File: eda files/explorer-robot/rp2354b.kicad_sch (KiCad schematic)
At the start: 34 parts, among them J1 Conn_01x03, SW1 SW_Push, U1 RP2354B, U2 AMS1117-3.3, Y1 ABM8-272-T3

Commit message: Add LiDAR power and UART interface
Add a new lidar schematic sheet with a 4-pin connector, an
AO3400A low-side MOSFET for power switching, and gate pull
resistors. Wire LIDAR_PWR, LIDAR_TX, and LIDAR_RX hierarchical
labels into the MCU sheet and update designators.

Also shorten connector value labels to BAT, LED, and MBR.
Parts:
- J1: value Conn_01x03 -> DBG
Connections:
- net LIDAR_RX: now reaches U1.11 (GPIO12)
- net LIDAR_PWR: now reaches U1.27 (GPIO26)
- net LIDAR_TX: now reaches U1.78 (GPIO1)
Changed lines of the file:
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@@
 	(wire
 		(pts
+			(xy 148.59 102.87) (xy 148.59 105.41)
+		)
+		(stroke
+			(width 0)
+			(type default)
+		)
+	)
+	(wire
+		(pts
 			(xy 264.16 33.02) (xy 264.16 34.29)
 		)
@@
 	(wire
 		(pts
+			(xy 184.15 102.87) (xy 184.15 105.41)
+		)
+		(stroke
+			(width 0)
+			(type default)
+		)
+	)
+	(wire
+		(pts
 			(xy 55.88 24.13) (xy 59.69 24.13)
 		)
@@
 	(wire
 		(pts
+			(xy 120.65 102.87) (xy 120.65 105.41)
+		)
+		(stroke
+			(width 0)
+			(type default)
+		)
+	)
+	(wire
+		(pts
 			(xy 123.19 31.75) (xy 130.81 31.75)
 		)
@@
 		)
 	)
+	(hierarchical_label "LIDAR_PWR"
+		(shape output)
+		(at 184.15 102.87 90)
+		(effects
+			(font
+				(size 1.27 1.27)
+			)
+			(justify left)
+		)
+	)
 	(hierarchical_label "ICM-20948_CS"
 		(shape output)
@@
 		)
 	)
+	(hierarchical_label "LIDAR_RX"
+		(shape output)
+		(at 148.59 102.87 90)
+		(effects
+			(font
+				(size 1.27 1.27)
+			)
+			(justify left)
+		)
+	)
 	(hierarchical_label "MOT.B.IN.2"
 		(shape output)
@@
 		)
 	)
+	(hierarchical_label "LIDAR_TX"
+		(shape input)
+		(at 120.65 102.87 90)
+		(effects
+			(font
+				(size 1.27 1.27)
+			)
+			(justify left)
+		)
+	)
 	(hierarchical_label "LED_R"
 		(shape output)
@@
 			)
 		)
-		(property "Value" "Conn_01x03"
+		(property "Value" "DBG"
 			(at 26.416 175.26 90)
 			(show_name no)

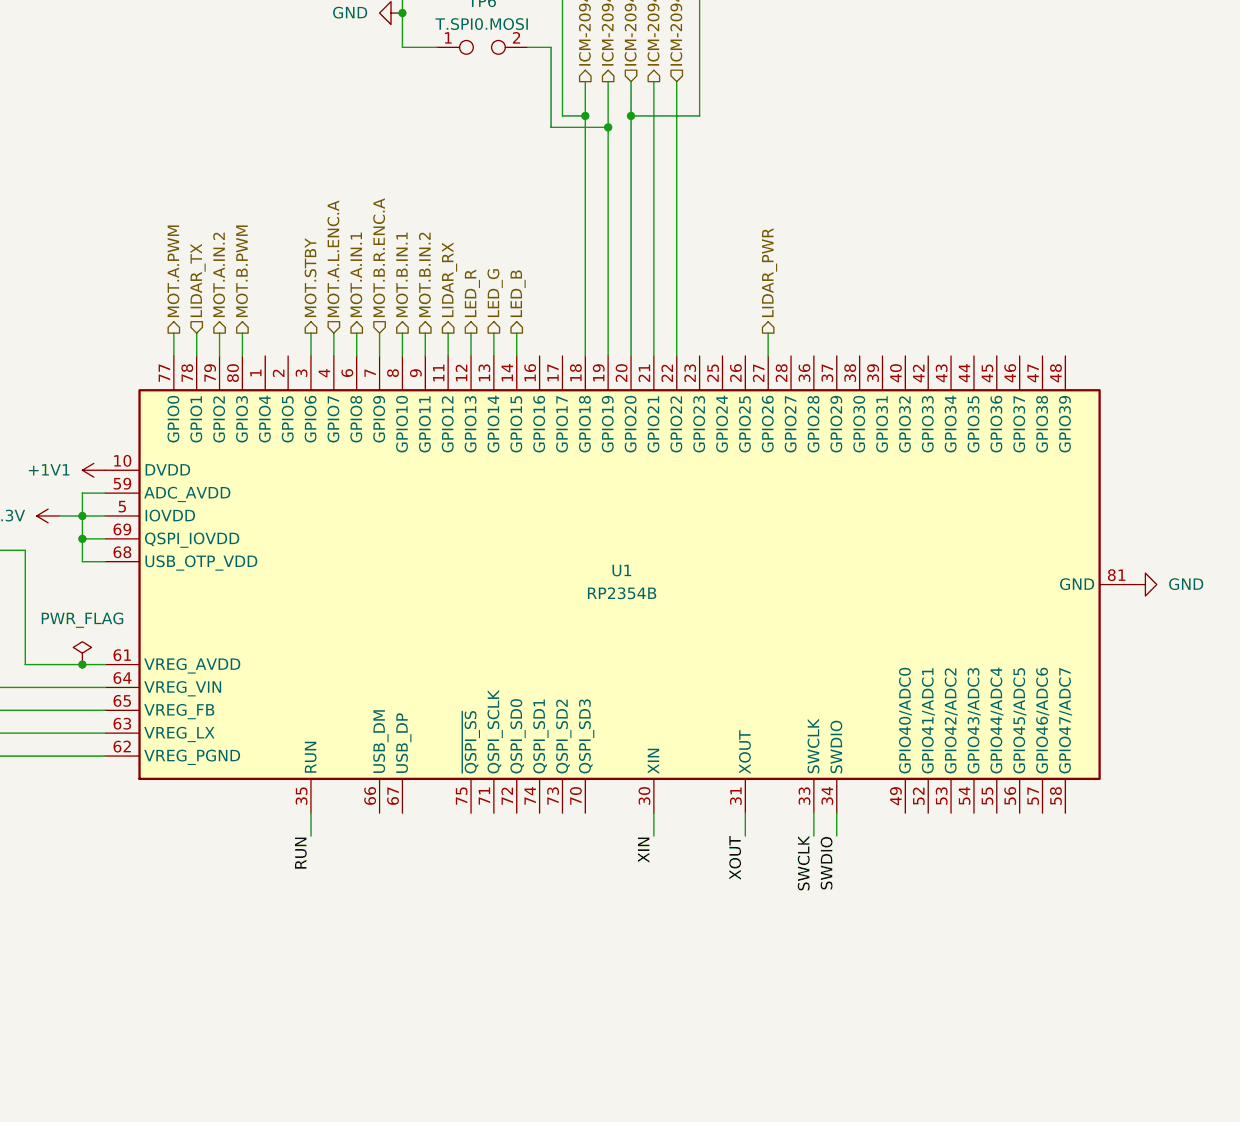
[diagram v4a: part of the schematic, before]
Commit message: Regroup RP2350B GPIOs by peripheral (ADR-0022)
Move motor/encoders to GPIO 4–12, LiDAR to 28–30, camera to 23–25
on a PIO0 UART, and reserve I2C1 on 26–27 for a second rangefinder.
Introduce assign_resources-based resource bundles so main splits the
embassy Peripherals in one call, and update docs, schematic and
firmware to the new pin map.
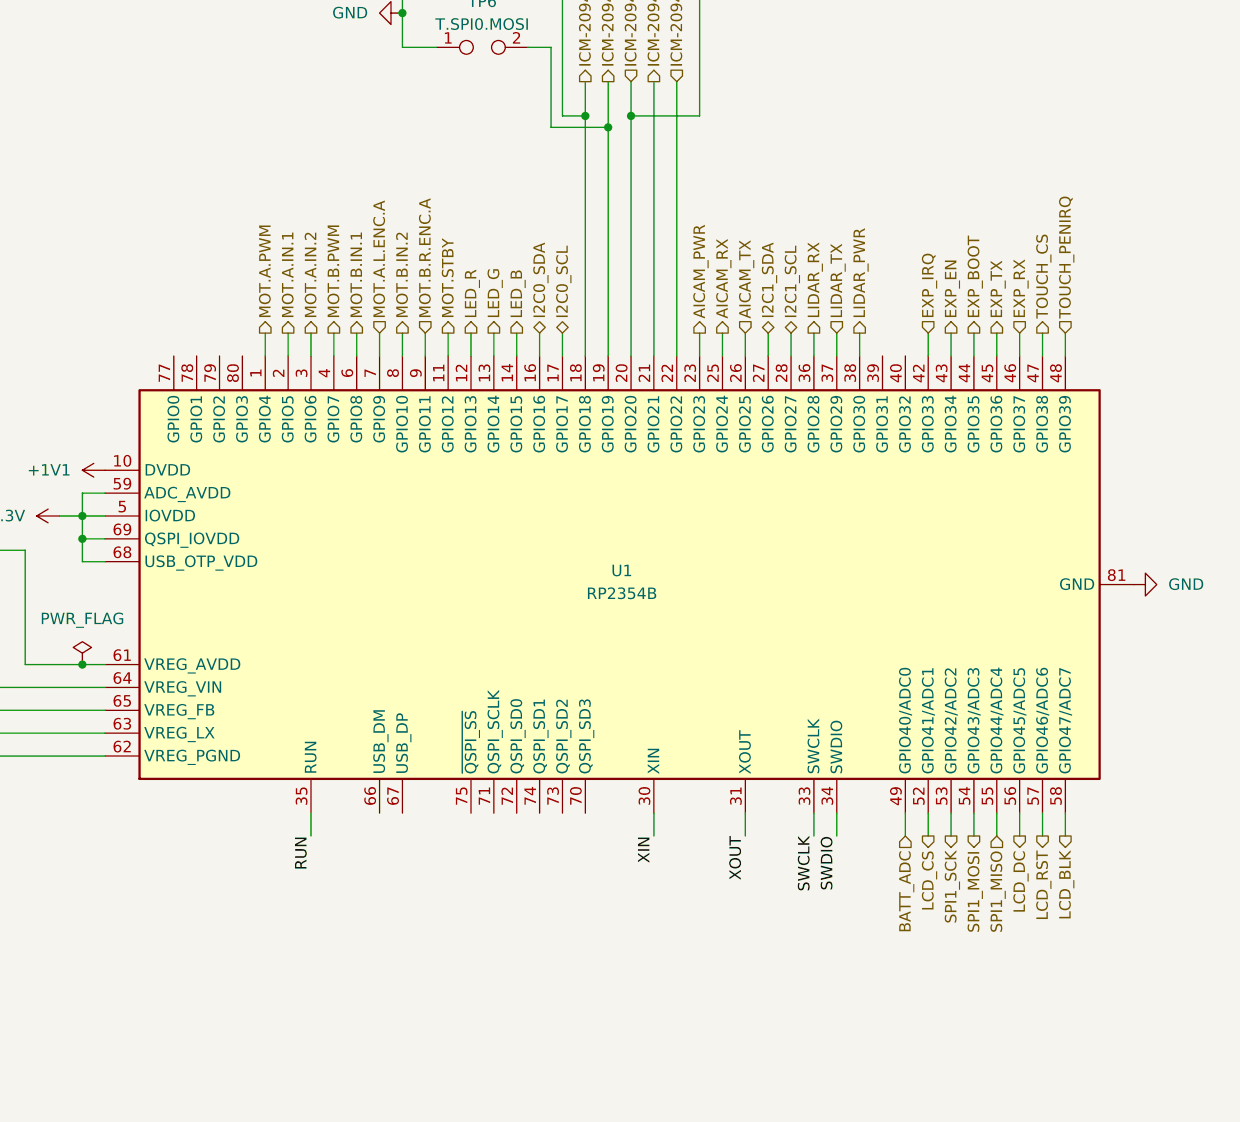
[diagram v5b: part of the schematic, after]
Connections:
- net LIDAR_PWR: now also U1.38 (GPIO30); no longer U1.27 (GPIO26)
- net LIDAR_RX: now also U1.36 (GPIO28); no longer U1.11 (GPIO12)
- net LIDAR_TX: now also U1.37 (GPIO29); no longer U1.78 (GPIO1)
- net MOT.A.IN.1: now also U1.2 (GPIO5); no longer U1.6 (GPIO8)
- net MOT.A.IN.2: now also U1.3 (GPIO6); no longer U1.79 (GPIO2)
- net MOT.A.L.ENC.A: now also U1.7 (GPIO9); no longer U1.4 (GPIO7)
- net MOT.A.PWM: now also U1.1 (GPIO4); no longer U1.77 (GPIO0)
- net MOT.B.IN.1: now also U1.6 (GPIO8); no longer U1.8 (GPIO10)
- net MOT.B.IN.2: now also U1.8 (GPIO10); no longer U1.9 (GPIO11)
- net MOT.B.PWM: now also U1.4 (GPIO7); no longer U1.80 (GPIO3)
- net MOT.B.R.ENC.A: now also U1.9 (GPIO11); no longer U1.7 (GPIO9)
- net MOT.STBY: now also U1.11 (GPIO12); no longer U1.3 (GPIO6)
- net I2C0_SDA: now reaches U1.16 (GPIO16)
- net I2C0_SCL: now reaches U1.17 (GPIO17)
- net AICAM_PWR: now reaches U1.23 (GPIO23)
- net AICAM_RX: now reaches U1.25 (GPIO24)
- net AICAM_TX: now reaches U1.26 (GPIO25)
- net I2C1_SCL: now reaches U1.28 (GPIO27)
- net EXP_IRQ: now reaches U1.42 (GPIO33)
- net EXP_EN: now reaches U1.43 (GPIO34)
- net EXP_BOOT: now reaches U1.44 (GPIO35)
- net EXP_TX: now reaches U1.45 (GPIO36)
- net EXP_RX: now reaches U1.46 (GPIO37)
- net TOUCH_CS: now reaches U1.47 (GPIO38)
- net TOUCH_PENIRQ: now reaches U1.48 (GPIO39)
- net BATT_ADC: now reaches U1.49 (GPIO40/ADC0)
- net LCD_CS: now reaches U1.52 (GPIO41/ADC1)
- net SPI1_SCK: now reaches U1.53 (GPIO42/ADC2)
- net SPI1_MOSI: now reaches U1.54 (GPIO43/ADC3)
- net SPI1_MISO: now reaches U1.55 (GPIO44/ADC4)
- net LCD_DC: now reaches U1.56 (GPIO45/ADC5)
- net LCD_RST: now reaches U1.57 (GPIO46/ADC6)
- net LCD_BLK: now reaches U1.58 (GPIO47/ADC7)
- new net I2C1_SDA: U1.27 (GPIO26)

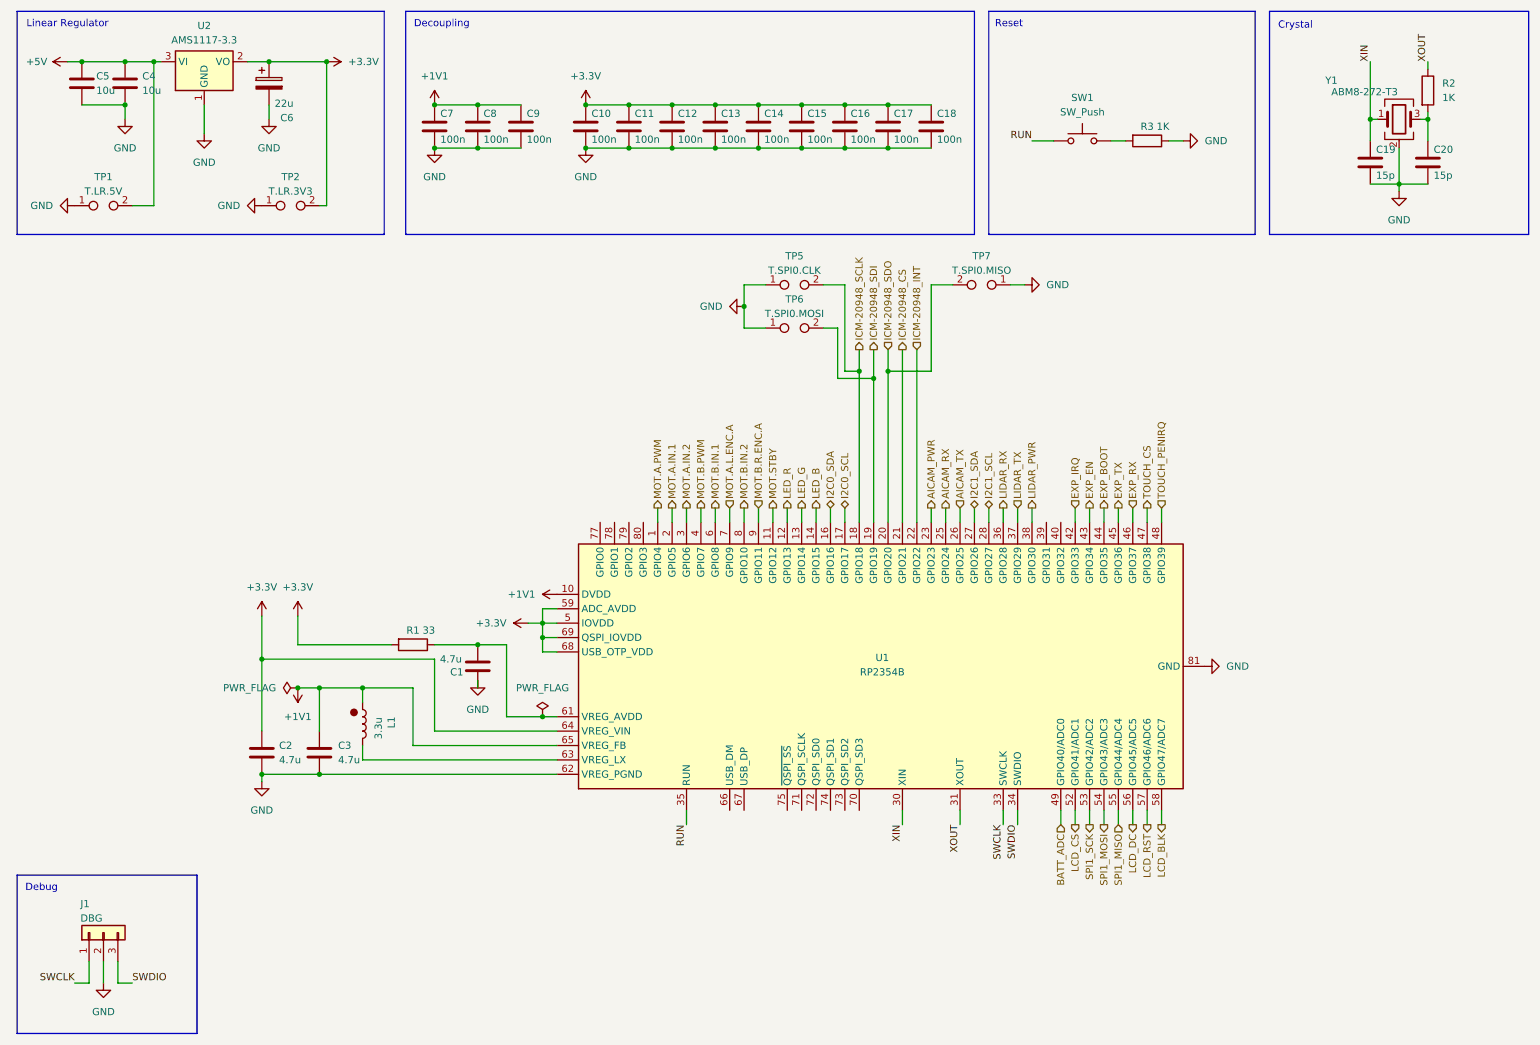
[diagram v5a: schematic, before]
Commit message: Add sheet titles and tidy RP2354B schematic layout
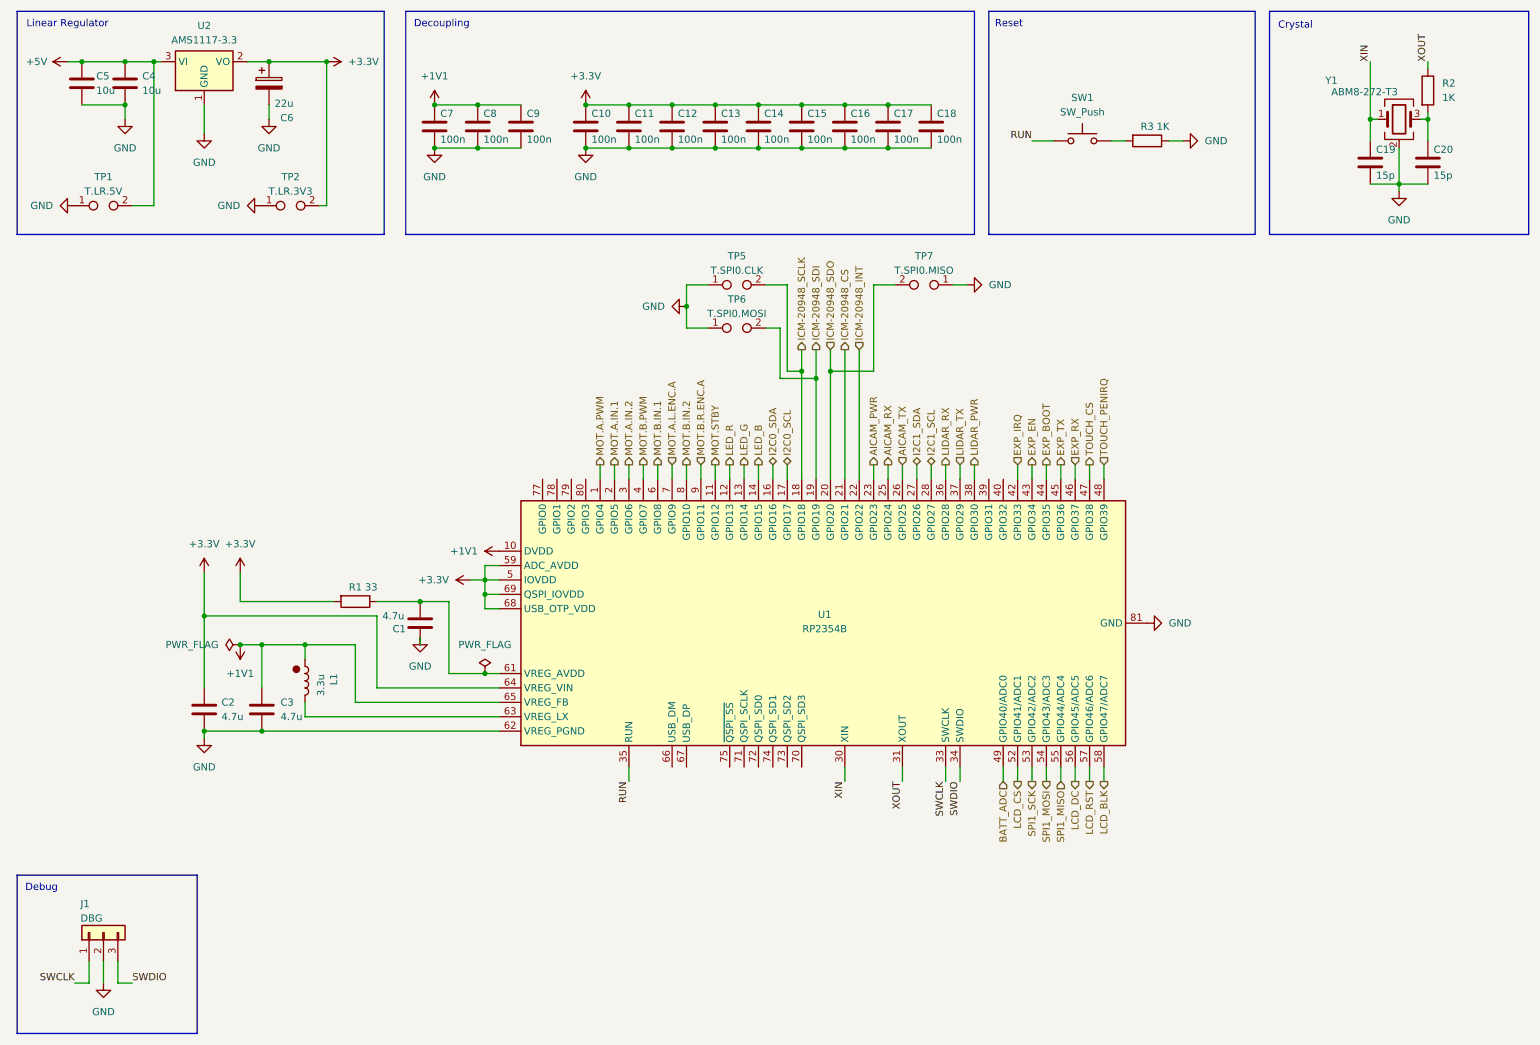
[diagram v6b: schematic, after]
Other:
- moved on the sheet: C1, C2, C3, L1, R1, TP5, TP6, TP7, U1

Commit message: Add AI CAM power switch and connector circuit
Adds a load switch, decoupling, UART series resistors, and JST
connector for the AI camera module, exposed via hierarchical
AICAM_RX/TX/PWR labels to the RP2354B.

Also drops the vendor name from the resources doc comment.
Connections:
- net EXP_PWR: now reaches U1.40 (GPIO32)
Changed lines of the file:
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@@
+	(wire
+		(pts
+			(xy 189.23 95.25) (xy 189.23 97.79)
+		)
+		(stroke
+			(width 0)
+			(type default)
+		)
+	)
 	(wire
 		(pts
@@
 		(effects
 			(font
+				(size 1.27 1.27)
+			)
+			(justify left)
+		)
+	)
+	(hierarchical_label "EXP_PWR"
+		(shape output)
+		(at 189.23 95.25 90)
+		(effects
+			(font

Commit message: Add switched 5 V panel branch with series resistors
The panel harness splits into PANEL.BUS (5 V, GND, shared SPI1 lines)
and
PANEL.CTRL (control lines) so a mis-plugged cable cannot short 5 V onto
a
3.3 V GPIO. A TPS22917 load switch on GPIO0 gates the panel's 5 V, and
series resistors (33 Ω on the 64 MHz SPI lines, 100 Ω on the slow
control
lines, 1 kΩ on TOUCH_PENIRQ) bound fault current and damp the bus.

GPIO0 leaves the spare pool; GPIO1–3 and GPIO31 remain spare. See
ADR-0024.
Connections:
- net PANEL_PWR: now reaches U1.77 (GPIO0)
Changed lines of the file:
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@@
+	(wire
+		(pts
+			(xy 107.95 95.25) (xy 107.95 97.79)
+		)
+		(stroke
+			(width 0)
+			(type default)
+		)
+	)
 	(wire
 		(pts
@@
 		(effects
 			(font
+				(size 1.27 1.27)
+			)
+			(justify left)
+		)
+	)
+	(hierarchical_label "PANEL_PWR"
+		(shape output)
+		(at 107.95 95.25 90)
+		(effects
+			(font
